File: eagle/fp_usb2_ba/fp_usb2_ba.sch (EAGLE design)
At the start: 9 parts, among them J1 M701-330442, J2 UJ2-AV-1-TH, J5 TSM-103-01-S-DV-A

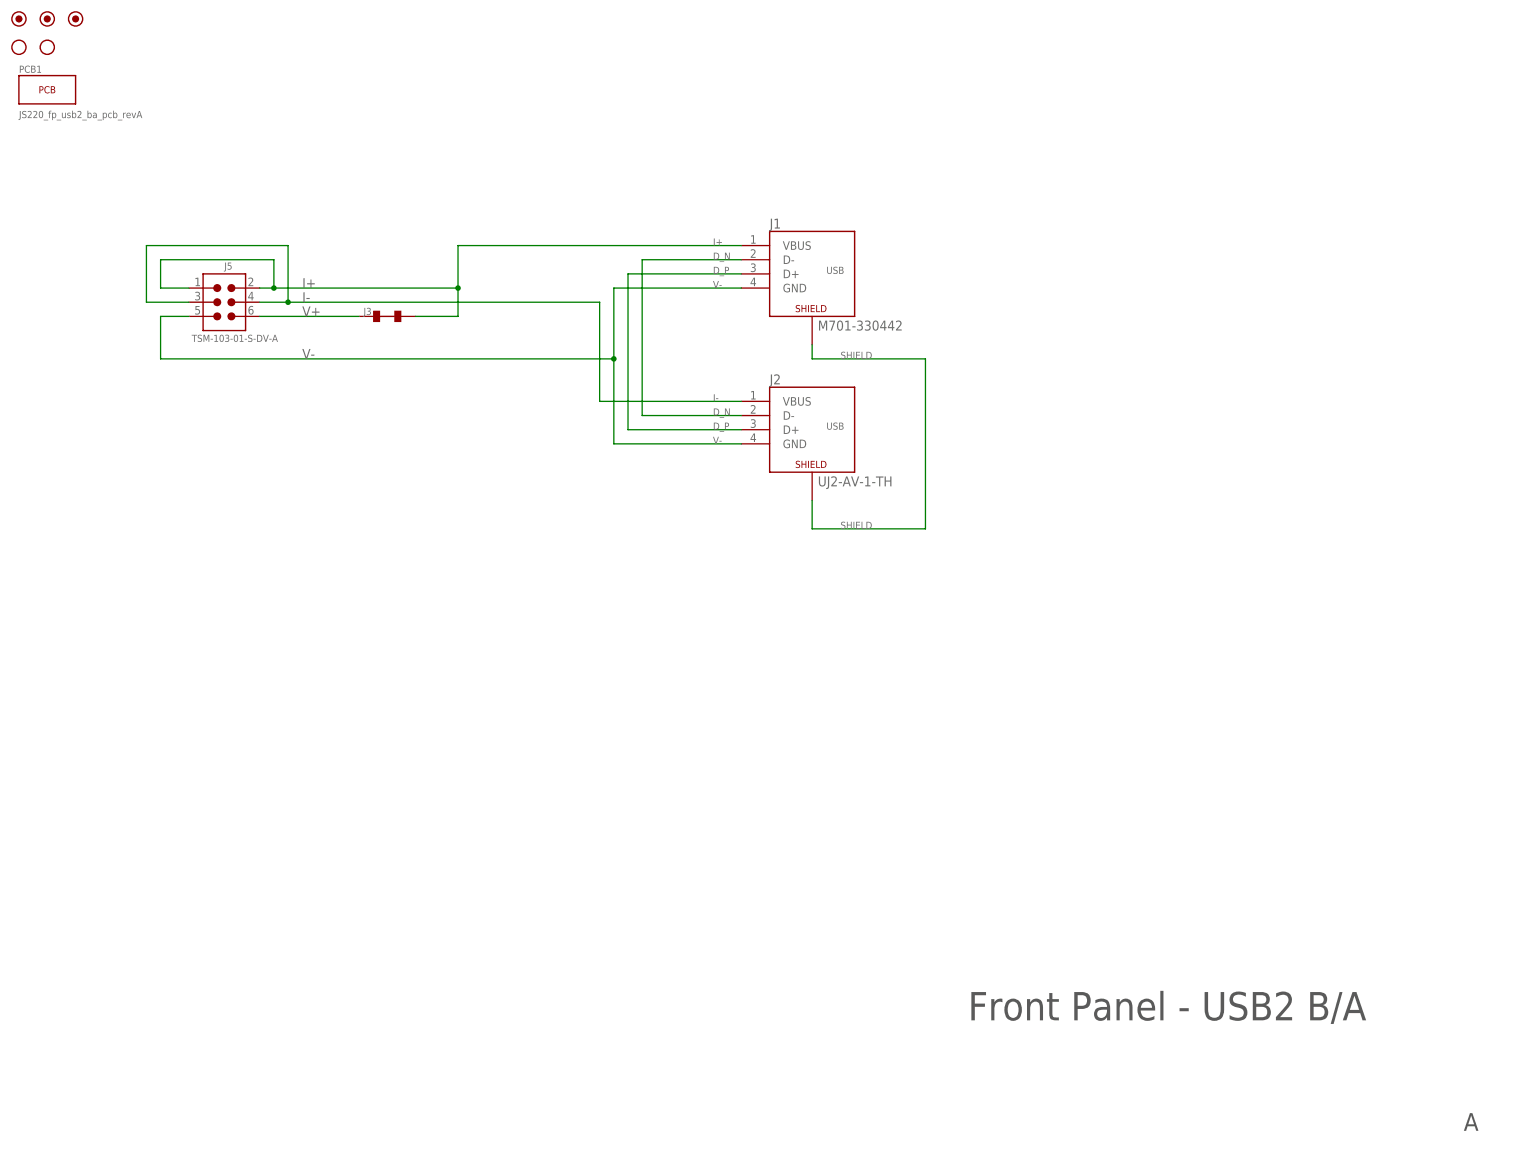
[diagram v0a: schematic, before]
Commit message: Fixed fb_usb2_ba connector A USB connector holes.
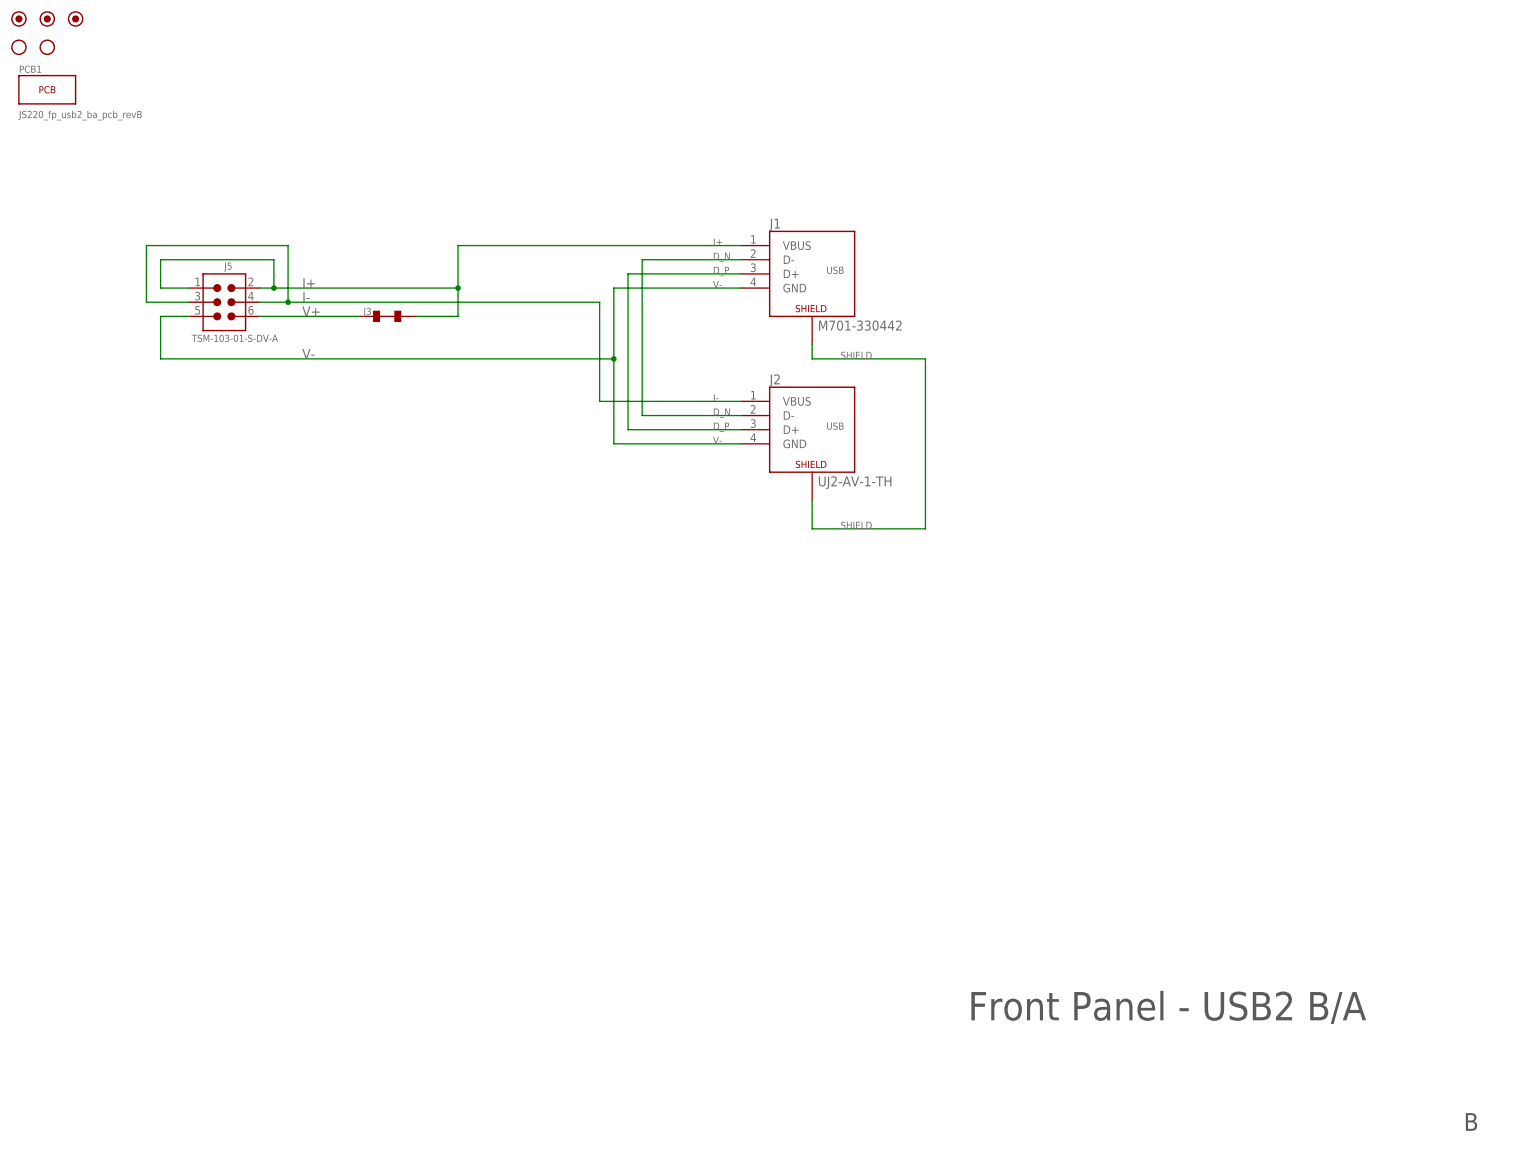
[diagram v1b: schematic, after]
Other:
- note added: "B"
- note removed: "A"
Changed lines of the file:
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@@
 <attribute name="POPULATE" value="0"/>
 </part>
-<part name="PCB1" library="jetperch" deviceset="PCB" device="" value="JS220_fp_usb2_ba_pcb_revA">
+<part name="PCB1" library="jetperch" deviceset="PCB" device="" value="JS220_fp_usb2_ba_pcb_revB">
 <attribute name="POPULATE" value="1"/>
 </part>
@@
 <plain>
 <text x="177.8" y="26.162" size="5.08" layer="97">Front Panel - USB2 B/A</text>
-<text x="266.7" y="6.35" size="3.175" layer="97">A</text>
+<text x="266.7" y="6.35" size="3.175" layer="97">B</text>
 </plain>
 <instances>
@@
 </sheet>
 </sheets>
+<errors>
+</errors>
 </schematic>
 </drawing>
